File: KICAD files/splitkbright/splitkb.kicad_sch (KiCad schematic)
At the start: 0 parts

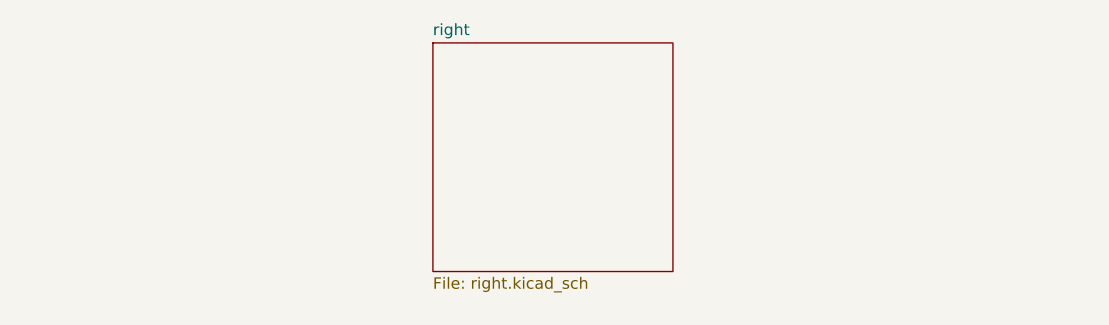
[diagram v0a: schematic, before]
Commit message: Edited PCB.
- Changed the footprint used for the dev board.
- Ran traces again for the dev board.
- Made a custom symbol and footprint for the devboard.
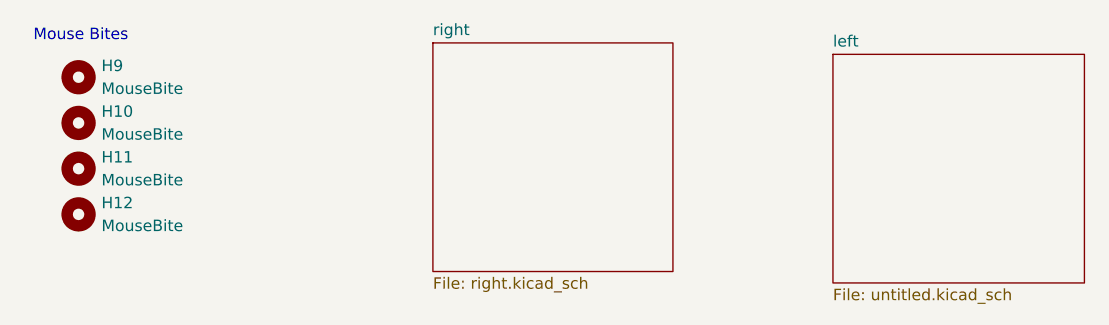
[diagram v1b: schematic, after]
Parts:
- added H10, H11, H12, H9: MouseBite, Panelization.pretty-master:mouse-bite-5mm-slot, symbol Mechanical:MountingHole
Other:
- added sheet left (untitled.kicad_sch)
- note added: "Mouse Bites"
